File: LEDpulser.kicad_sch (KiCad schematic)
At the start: 70 parts, among them J1 RJHSE-5380, J2 EPS.00.250.NTN, J3 EPS.00.250.NTN, J4 EB21A-04-D, J5 EPL.0S.302.HLN, Q1 BVSS84LT1G, Q2 DMN3028LQ-7, Q3 DMN3028LQ-7, SW1 BST11T2AVR, U1 74AHCT123APW,118, U10 LT3082EST#TRPBF, U2 74AHCT123APW,118, U3 74AHCT123APW,118, U4 SN74LVC2G74, U5 LT1121CST-5#TRPBF, U6 IXDI602SIATR, U7 NE555S-13, U8 PM8834, U9 PM8834

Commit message: Routed
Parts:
- RV5: value 50k -> 100k; Part# 3262X-1-503LF -> 3296Z-1-104LF
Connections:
- net LED_ON: now also U8.4 (IN_B); no longer U8.2 (IN_A)
- net LED_ON_OUT: now also U8.5 (OUT_B); no longer U8.7 (OUT_A)
- net LED_SHORT: now also U8.2 (IN_A); no longer U8.4 (IN_B)
- net LED_SHORT_OUT: now also U8.7 (OUT_A); no longer U8.5 (OUT_B)
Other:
- moved on the sheet: C16, C17
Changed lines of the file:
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@@
   (junction (at 42.545 164.465) (diameter 0) (color 0 0 0 0)
   )
+  (junction (at 278.13 157.48) (diameter 0) (color 0 0 0 0)
+  )
   (junction (at 134.62 107.95) (diameter 0) (color 0 0 0 0)
   )
@@
   (junction (at 71.12 185.42) (diameter 0) (color 0 0 0 0)
   )
-  (junction (at 285.75 119.38) (diameter 0) (color 0 0 0 0)
+  (junction (at 285.75 157.48) (diameter 0) (color 0 0 0 0)
   )
   (junction (at 197.485 135.89) (diameter 0) (color 0 0 0 0)
@@
   (junction (at 60.96 120.015) (diameter 0) (color 0 0 0 0)
   )
-  (junction (at 278.13 119.38) (diameter 0) (color 0 0 0 0)
-  )
   (junction (at 65.405 105.41) (diameter 0) (color 0 0 0 0)
   )
@@
     (stroke (width 0) (type default) (color 0 0 0 0))
   )
-  (wire (pts (xy 272.415 119.38) (xy 278.13 119.38))
+  (wire (pts (xy 272.415 157.48) (xy 278.13 157.48))
     (stroke (width 0) (type default) (color 0 0 0 0))
   )
@@
     (stroke (width 0) (type default) (color 0 0 0 0))
   )
-  (wire (pts (xy 278.13 119.38) (xy 285.75 119.38))
-    (stroke (width 0) (type default) (color 0 0 0 0))
-  )
   (wire (pts (xy 100.965 96.52) (xy 100.965 92.71))
     (stroke (width 0) (type default) (color 0 0 0 0))
@@
     (stroke (width 0) (type default) (color 0 0 0 0))
   )
-  (wire (pts (xy 285.75 118.745) (xy 285.75 119.38))
+  (wire (pts (xy 285.75 158.115) (xy 285.75 157.48))
     (stroke (width 0) (type default) (color 0 0 0 0))
   )
@@
     (stroke (width 0) (type default) (color 0 0 0 0))
   )
-  (wire (pts (xy 285.75 119.38) (xy 285.75 128.27))
+  (wire (pts (xy 285.75 157.48) (xy 285.75 148.59))
     (stroke (width 0) (type default) (color 0 0 0 0))
   )
@@
     (stroke (width 0) (type default) (color 0 0 0 0))
   )
+  (wire (pts (xy 278.13 157.48) (xy 285.75 157.48))
+    (stroke (width 0) (type default) (color 0 0 0 0))
+  )
   (wire (pts (xy 264.16 135.89) (xy 275.59 135.89))
     (stroke (width 0) (type default) (color 0 0 0 0))
@@
     (pin "1")
   )
-  (symbol (lib_id "Device:C") (at 278.13 123.19 0) (unit 1)
+  (symbol (lib_id "Device:C") (at 278.13 161.29 0) (mirror y) (unit 1)
     (in_bom yes) (on_board yes)
-    (property "Reference" "C17" (id 0) (at 280.035 125.73 0)
-      (effects (font (size 1.27 1.27)) (justify left))
+    (property "Reference" "C17" (id 0) (at 280.035 164.465 0)
+      (effects (font (size 1.27 1.27)) (justify right))
     )
-    (property "Value" "0.1uF" (id 1) (at 280.035 127.635 0)
-      (effects (font (size 1.27 1.27)) (justify left))
+    (property "Value" "0.1uF" (id 1) (at 280.035 166.37 0)
+      (effects (font (size 1.27 1.27)) (justify right))
     )
-    (property "Footprint" "Capacitor_SMD:C_0603_1608Metric" (id 2) (at 279.0952 127 0)
+    (property "Footprint" "Capacitor_SMD:C_0603_1608Metric" (id 2) (at 277.1648 165.1 0)
       (effects (font (size 1.27 1.27)) hide)
     )
-    (property "Datasheet" "~" (id 3) (at 278.13 123.19 0)
+    (property "Datasheet" "~" (id 3) (at 278.13 161.29 0)
       (effects (font (size 1.27 1.27)) hide)
     )
@@
     (in_bom yes) (on_board yes)
     (property "Reference" "RV5" (id 0) (at 67.945 115.57 90))
-    (property "Value" "50k" (id 1) (at 65.405 115.57 90))
+    (property "Value" "100k" (id 1) (at 65.405 115.57 90))
     (property "Footprint" "Potentiometer_THT:Potentiometer_Bourns_3266X_Horizontal" (id 2) (at 65.405 115.57 0)
       (effects (font (size 1.27 1.27)) hide)
@@
       (effects (font (size 1.27 1.27)) hide)
     )
-    (property "Part#" "3262X-1-503LF" (id 4) (at 65.405 115.57 0)
+    (property "Part#" "3296Z-1-104LF" (id 4) (at 65.405 115.57 0)
       (effects (font (size 1.27 1.27)) hide)
     )
@@
     (pin "2")
   )
-  (symbol (lib_id "Driver_FET:EL7202CN") (at 285.75 138.43 0) (unit 1)
+  (symbol (lib_id "Driver_FET:EL7202CN") (at 285.75 138.43 0) (mirror x) (unit 1)
     (in_bom yes) (on_board yes) (fields_autoplaced)
-    (property "Reference" "U8" (id 0) (at 287.7694 126.8435 0)
+    (property "Reference" "U8" (id 0) (at 287.7694 150.0165 0)
       (effects (font (size 1.27 1.27)) (justify left))
     )
-    (property "Value" "PM8834" (id 1) (at 287.7694 129.6186 0)
+    (property "Value" "PM8834" (id 1) (at 287.7694 147.2414 0)
       (effects (font (size 1.27 1.27)) (justify left))
     )
-    (property "Footprint" "Package_SO:SO-8_3.9x4.9mm_P1.27mm" (id 2) (at 285.75 146.05 0)
+    (property "Footprint" "Package_SO:SO-8_3.9x4.9mm_P1.27mm" (id 2) (at 285.75 130.81 0)
       (effects (font (size 1.27 1.27)) hide)
     )
-    (property "Datasheet" "https://www.st.com/content/ccc/resource/technical/document/datasheet/9a/22/3e/55/d3/f8/46/d5/CD00212712.pdf/files/CD00212712.pdf/jcr:content/translations/en.CD00212712.pdf" (id 3) (at 285.75 146.05 0)
+    (property "Datasheet" "https://www.st.com/content/ccc/resource/technical/document/datasheet/9a/22/3e/55/d3/f8/46/d5/CD00212712.pdf/files/CD00212712.pdf/jcr:content/translations/en.CD00212712.pdf" (id 3) (at 285.75 130.81 0)
       (effects (font (size 1.27 1.27)) hide)
     )
@@
     (pin "1")
   )
-  (symbol (lib_id "power:GND") (at 272.415 127 0) (unit 1)
+  (symbol (lib_id "power:GND") (at 272.415 165.1 0) (mirror y) (unit 1)
     (in_bom yes) (on_board yes) (fields_autoplaced)
-    (property "Reference" "#PWR0152" (id 0) (at 272.415 133.35 0)
+    (property "Reference" "#PWR0152" (id 0) (at 272.415 171.45 0)
       (effects (font (size 1.27 1.27)) hide)
     )
-    (property "Value" "GND" (id 1) (at 274.32 128.749 0)
+    (property "Value" "GND" (id 1) (at 270.51 166.849 0)
       (effects (font (size 1.27 1.27)) (justify left) hide)
     )
-    (property "Footprint" "" (id 2) (at 272.415 127 0)
+    (property "Footprint" "" (id 2) (at 272.415 165.1 0)
       (effects (font (size 1.27 1.27)) hide)
     )
-    (property "Datasheet" "" (id 3) (at 272.415 127 0)
+    (property "Datasheet" "" (id 3) (at 272.415 165.1 0)
       (effects (font (size 1.27 1.27)) hide)
     )
@@
     (pin "3")
   )
-  (symbol (lib_id "power:GND") (at 278.13 127 0) (unit 1)
+  (symbol (lib_id "power:GND") (at 278.13 165.1 0) (mirror y) (unit 1)
     (in_bom yes) (on_board yes) (fields_autoplaced)
-    (property "Reference" "#PWR0151" (id 0) (at 278.13 133.35 0)
+    (property "Reference" "#PWR0151" (id 0) (at 278.13 171.45 0)
       (effects (font (size 1.27 1.27)) hide)
     )
-    (property "Value" "GND" (id 1) (at 280.035 128.749 0)
+    (property "Value" "GND" (id 1) (at 276.225 166.849 0)
       (effects (font (size 1.27 1.27)) (justify left) hide)
     )
-    (property "Footprint" "" (id 2) (at 278.13 127 0)
+    (property "Footprint" "" (id 2) (at 278.13 165.1 0)
       (effects (font (size 1.27 1.27)) hide)
     )
-    (property "Datasheet" "" (id 3) (at 278.13 127 0)
+    (property "Datasheet" "" (id 3) (at 278.13 165.1 0)
       (effects (font (size 1.27 1.27)) hide)
     )
@@
     (pin "1")
   )
-  (symbol (lib_id "Device:C") (at 272.415 123.19 0) (unit 1)
+  (symbol (lib_id "Device:C") (at 272.415 161.29 0) (mirror y) (unit 1)
     (in_bom yes) (on_board yes)
-    (property "Reference" "C16" (id 0) (at 271.78 118.745 0)
-      (effects (font (size 1.27 1.27)) (justify right))
+    (property "Reference" "C16" (id 0) (at 271.78 156.845 0)
+      (effects (font (size 1.27 1.27)) (justify left))
     )
-    (property "Value" "1uF" (id 1) (at 271.78 120.65 0)
-      (effects (font (size 1.27 1.27)) (justify right))
+    (property "Value" "1uF" (id 1) (at 271.78 158.75 0)
+      (effects (font (size 1.27 1.27)) (justify left))
     )
-    (property "Footprint" "Capacitor_SMD:C_0603_1608Metric" (id 2) (at 273.3802 127 0)
+    (property "Footprint" "Capacitor_SMD:C_0603_1608Metric" (id 2) (at 271.4498 165.1 0)
       (effects (font (size 1.27 1.27)) hide)
     )
-    (property "Datasheet" "~" (id 3) (at 272.415 123.19 0)
+    (property "Datasheet" "~" (id 3) (at 272.415 161.29 0)
       (effects (font (size 1.27 1.27)) hide)
     )
@@
     (pin "1")
   )
-  (symbol (lib_id "power:GND") (at 285.75 148.59 0) (unit 1)
+  (symbol (lib_id "power:GND") (at 285.75 128.27 0) (mirror x) (unit 1)
     (in_bom yes) (on_board yes) (fields_autoplaced)
-    (property "Reference" "#PWR0150" (id 0) (at 285.75 154.94 0)
+    (property "Reference" "#PWR0150" (id 0) (at 285.75 121.92 0)
       (effects (font (size 1.27 1.27)) hide)
     )
-    (property "Value" "GND" (id 1) (at 285.75 153.1525 0)
+    (property "Value" "GND" (id 1) (at 285.75 123.7075 0)
       (effects (font (size 1.27 1.27)) hide)
     )
-    (property "Footprint" "" (id 2) (at 285.75 148.59 0)
+    (property "Footprint" "" (id 2) (at 285.75 128.27 0)
       (effects (font (size 1.27 1.27)) hide)
     )
-    (property "Datasheet" "" (id 3) (at 285.75 148.59 0)
+    (property "Datasheet" "" (id 3) (at 285.75 128.27 0)
       (effects (font (size 1.27 1.27)) hide)
     )
@@
     (pin "1")
   )
-  (symbol (lib_id "power:VCC") (at 285.75 118.745 0) (unit 1)
+  (symbol (lib_id "power:VCC") (at 285.75 158.115 0) (mirror x) (unit 1)
     (in_bom yes) (on_board yes)
-    (property "Reference" "#PWR021" (id 0) (at 285.75 122.555 0)
+    (property "Reference" "#PWR021" (id 0) (at 285.75 154.305 0)
       (effects (font (size 1.27 1.27)) hide)
     )
-    (property "Value" "VCC" (id 1) (at 285.75 114.935 0))
-    (property "Footprint" "" (id 2) (at 285.75 118.745 0)
+    (property "Value" "VCC" (id 1) (at 285.75 161.925 0))
+    (property "Footprint" "" (id 2) (at 285.75 158.115 0)
       (effects (font (size 1.27 1.27)) hide)
     )
-    (property "Datasheet" "" (id 3) (at 285.75 118.745 0)
+    (property "Datasheet" "" (id 3) (at 285.75 158.115 0)
       (effects (font (size 1.27 1.27)) hide)
     )
@@
     )
     (path "/2bd507de-9da7-4407-a155-fc7ba55ac707"
-      (reference "RV5") (unit 1) (value "50k") (footprint "Potentiometer_THT:Potentiometer_Bourns_3266X_Horizontal")
+      (reference "RV5") (unit 1) (value "100k") (footprint "Potentiometer_THT:Potentiometer_Bourns_3266X_Horizontal")
     )
     (path "/17f0aa36-8ef2-4e70-843d-08846cd7493b"

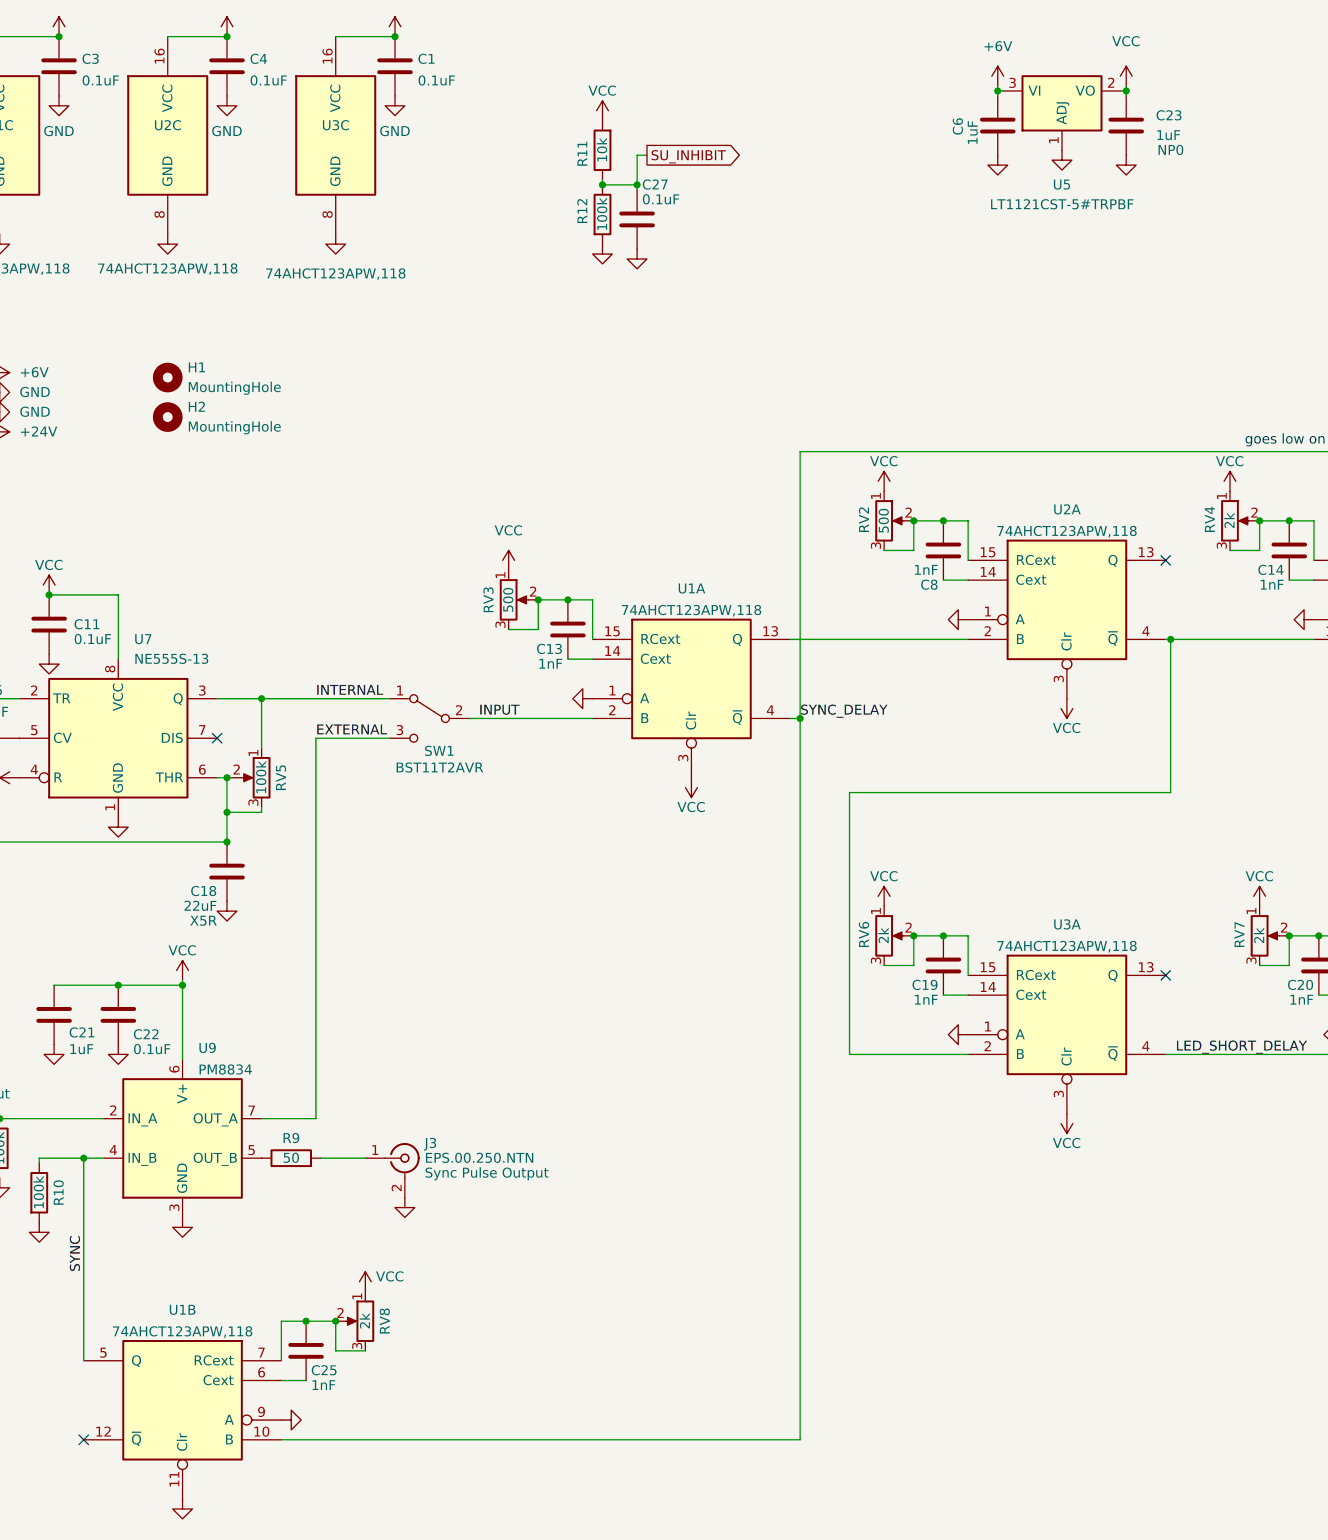
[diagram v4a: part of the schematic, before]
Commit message: Fixed enable for sync pulse monostable
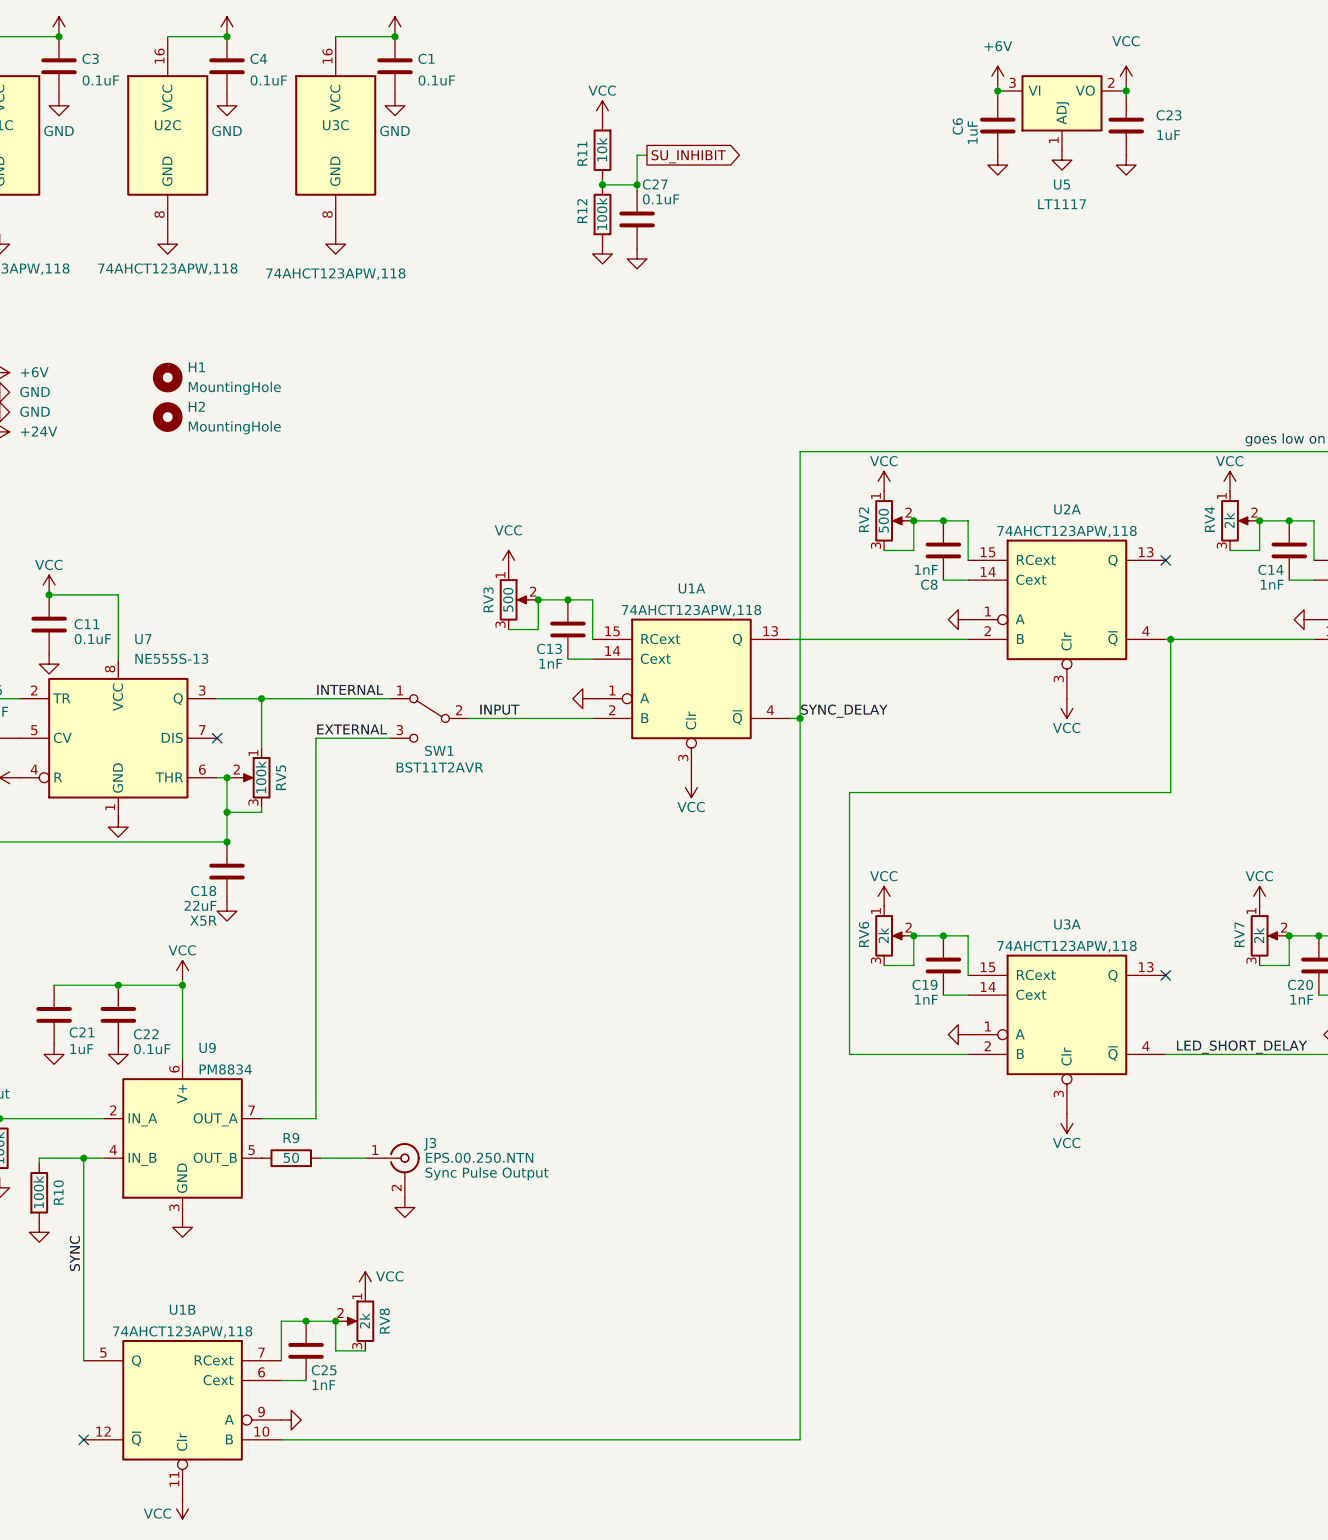
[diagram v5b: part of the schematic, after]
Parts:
- C23: Dielectric NP0 -> (none)
- U5: value LT1121CST-5#TRPBF -> LT1117
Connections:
- net GND: no longer U1.11 (Clr)
- net VCC: now also U1.11 (Clr)
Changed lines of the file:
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@@
+    (pin "1")
+  )
+  (symbol (lib_id "power:VCC") (at 55.245 208.28 180) (unit 1)
+    (in_bom yes) (on_board yes)
+    (property "Reference" "#PWR?" (id 0) (at 55.245 204.47 0)
+      (effects (font (size 1.27 1.27)) hide)
+    )
+    (property "Value" "VCC" (id 1) (at 52.07 210.185 0))
+    (property "Footprint" "" (id 2) (at 55.245 208.28 0)
+      (effects (font (size 1.27 1.27)) hide)
+    )
+    (property "Datasheet" "" (id 3) (at 55.245 208.28 0)
+      (effects (font (size 1.27 1.27)) hide)
+    )
     (pin "1")
   )
@@
       (effects (font (size 1.27 1.27)) hide)
     )
-    (property "Dielectric" "NP0" (id 4) (at 182.245 34.925 0))
+    (property "Dielectric" "" (id 4) (at 182.245 34.925 0)
+      (effects (font (size 1.27 1.27)) hide)
+    )
     (pin "1")
     (pin "2")
@@
     (pin "1")
   )
-  (symbol (lib_id "power:GND") (at 55.245 208.28 0) (mirror y) (unit 1)
-    (in_bom yes) (on_board yes) (fields_autoplaced)
-    (property "Reference" "#PWR0179" (id 0) (at 55.245 214.63 0)
-      (effects (font (size 1.27 1.27)) hide)
-    )
-    (property "Value" "GND" (id 1) (at 53.34 209.5499 0)
-      (effects (font (size 1.27 1.27)) (justify left) hide)
-    )
-    (property "Footprint" "" (id 2) (at 55.245 208.28 0)
-      (effects (font (size 1.27 1.27)) hide)
-    )
-    (property "Datasheet" "" (id 3) (at 55.245 208.28 0)
-      (effects (font (size 1.27 1.27)) hide)
-    )
-    (pin "1")
-  )
   (symbol (lib_id "Device:C") (at 153.035 139.7 0) (unit 1)
     (in_bom yes) (on_board yes)
@@
     (in_bom yes) (on_board yes)
     (property "Reference" "U5" (id 0) (at 168.275 39.37 0))
-    (property "Value" "LT1121CST-5#TRPBF" (id 1) (at 168.275 41.91 0))
+    (property "Value" "LT1117" (id 1) (at 168.275 41.91 0))
     (property "Footprint" "Package_TO_SOT_SMD:SOT-223-3_TabPin2" (id 2) (at 168.275 27.305 0)
       (effects (font (size 1.27 1.27)) hide)
     )
-    (property "Datasheet" "https://www.analog.com/media/en/technical-documentation/data-sheets/1121fg.pdf" (id 3) (at 168.275 27.305 0)
+    (property "Datasheet" "https://www.analog.com/media/en/technical-documentation/data-sheets/1117fd.pdf" (id 3) (at 168.275 27.305 0)
       (effects (font (size 1.27 1.27)) hide)
     )
@@
       (reference "#PWR0177") (unit 1) (value "GND") (footprint "")
     )
-    (path "/6bc00599-0e61-434b-9132-bb199a859ad9"
-      (reference "#PWR0179") (unit 1) (value "GND") (footprint "")
+    (path "/3407777c-d948-490d-a2f0-b3ad3390e217"
+      (reference "#PWR?") (unit 1) (value "VCC") (footprint "")
     )
     (path "/f93b1b9a-0026-469f-bb79-98b3a8c675dd"
@@
     )
     (path "/9a7be1d6-c29d-40a4-8942-1e5028d740eb"
-      (reference "U5") (unit 1) (value "LT1121CST-5#TRPBF") (footprint "Package_TO_SOT_SMD:SOT-223-3_TabPin2")
+      (reference "U5") (unit 1) (value "LT1117") (footprint "Package_TO_SOT_SMD:SOT-223-3_TabPin2")
     )
     (path "/d767f2ff-12ec-4778-96cb-3fdd7a473d60"
